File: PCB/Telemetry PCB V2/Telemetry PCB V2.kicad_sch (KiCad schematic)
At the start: 47 parts, among them IC1 E22-900M22S, J1 USB_C_Receptacle_USB2.0_16P, J2 DBG/PGRM Hdr., J3 DATA IN, J4 GPS, J5 Battery, SW1 SW_MEC_5E, SW2 SW_MEC_5E, U1 STM32F411CEUx, U2 MCP1700x-250xxTT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

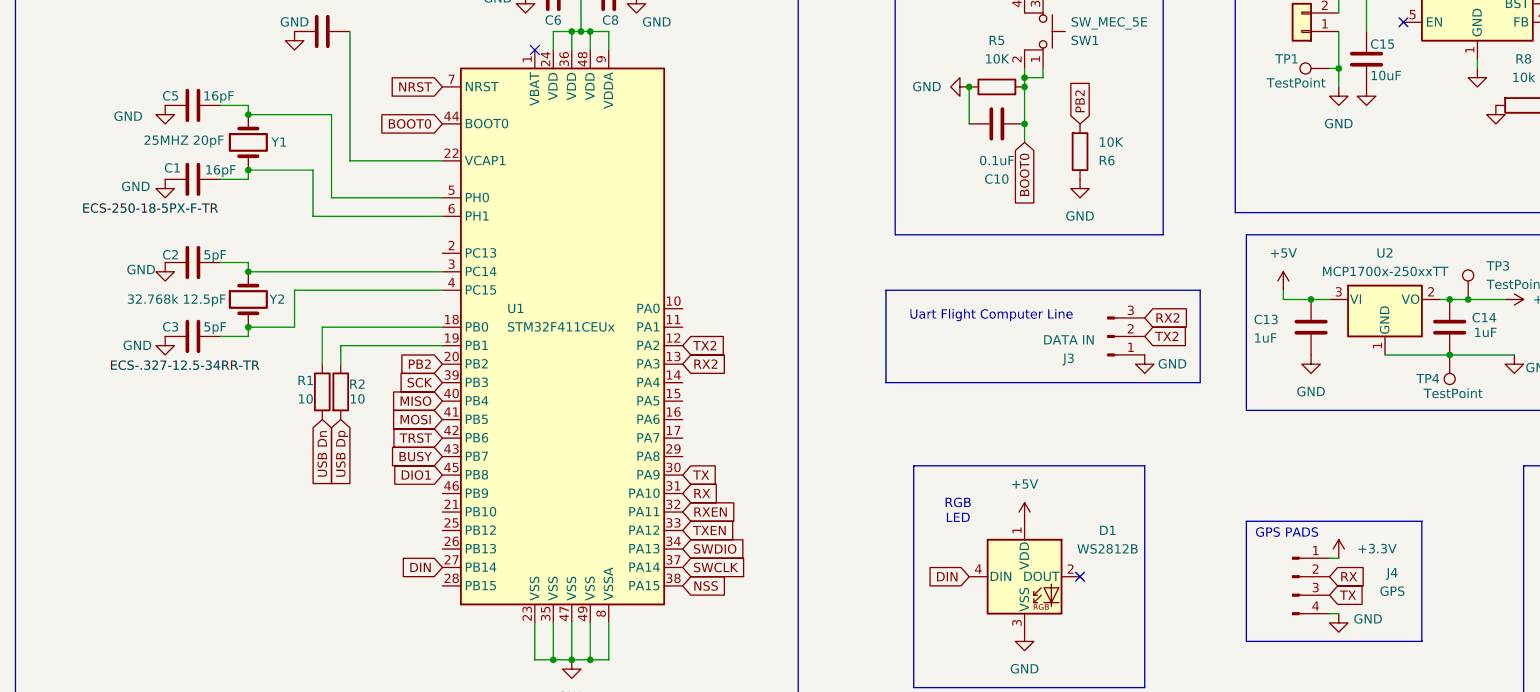
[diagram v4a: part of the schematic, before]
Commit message: Changed GPS power to 5V
Changed GPS power to 5V because I was not sure what it's current draw is and we don't have a ton of spare capacity on the 3.3V power regulator. Powering of of 5V is also likely more power efficient as it is not passing through a linear voltage regulator
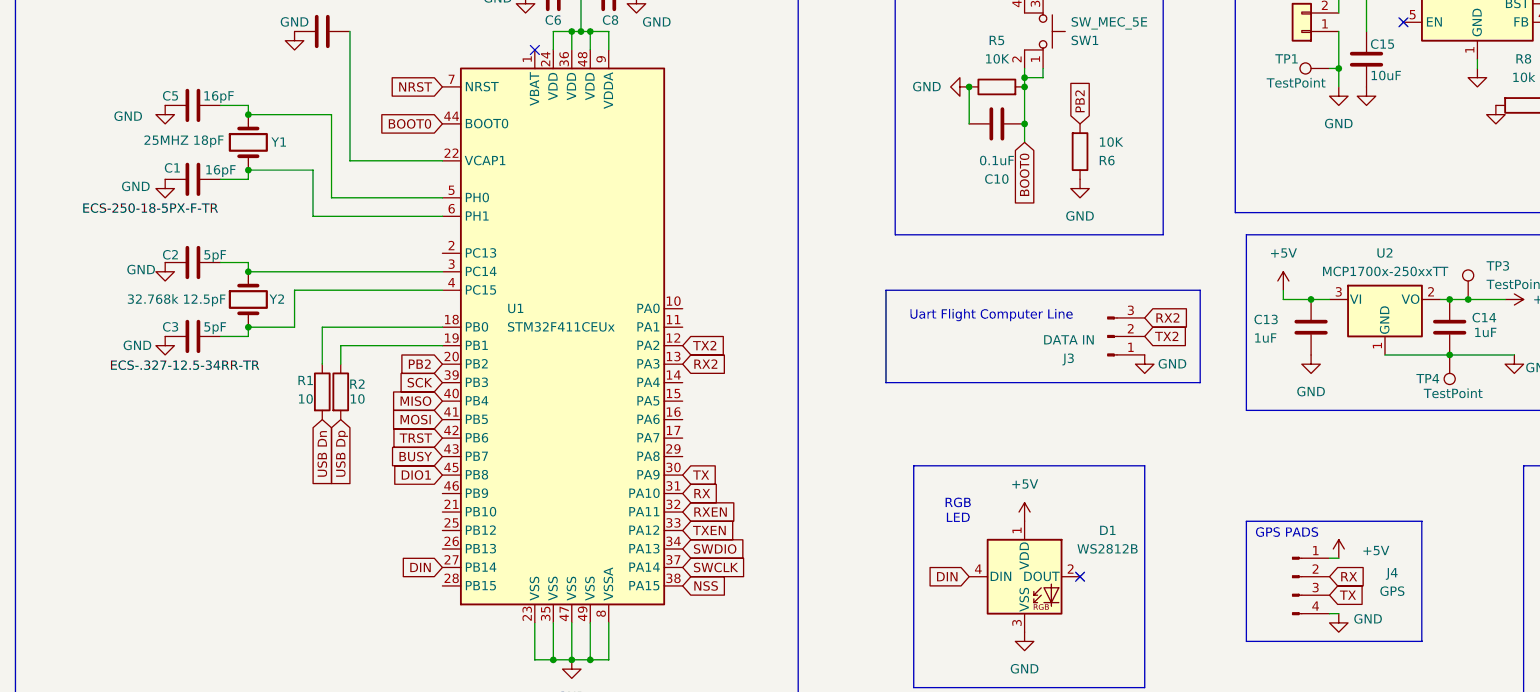
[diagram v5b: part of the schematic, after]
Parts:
- Y1: value 25MHZ 20pF -> 25MHZ 18pF
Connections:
- net +3.3V: no longer J4.1 (Pin_1)
- net +5V: now also J4.1 (Pin_1)
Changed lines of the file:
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@@
 			)
 		)
-		(property "Value" "25MHZ 20pF"
+		(property "Value" "25MHZ 18pF"
 			(at 53.848 48.006 90)
 			(effects
@@
 	)
 	(symbol
+		(lib_id "power:+5V")
+		(at 207.01 105.41 0)
+		(unit 1)
+		(exclude_from_sim no)
+		(in_bom yes)
+		(on_board yes)
+		(dnp no)
+		(property "Reference" "#PWR011"
+			(at 207.01 109.22 0)
+			(effects
+				(font
+					(size 1.27 1.27)
+				)
+				(hide yes)
+			)
+		)
+		(property "Value" "+5V"
+			(at 212.09 104.394 0)
+			(effects
+				(font
+					(size 1.27 1.27)
+				)
+			)
+		)
+		(property "Footprint" ""
+			(at 207.01 105.41 0)
+			(effects
+				(font
+					(size 1.27 1.27)
+				)
+				(hide yes)
+			)
+		)
+		(property "Datasheet" ""
+			(at 207.01 105.41 0)
+			(effects
+				(font
+					(size 1.27 1.27)
+				)
+				(hide yes)
+			)
+		)
+		(property "Description" "Power symbol creates a global label with name \"+5V\""
+			(at 207.01 105.41 0)
+			(effects
+				(font
+					(size 1.27 1.27)
+				)
+				(hide yes)
+			)
+		)
+		(pin "1"
+		)
+		(instances
+			(project ""
+				(path "/d3e58202-7594-4bd8-a3d4-cb0300333d9c"
+					(reference "#PWR011")
+					(unit 1)
+				)
+			)
+		)
+	)
+	(symbol
 		(lib_name "+3.3V_3")
 		(lib_id "power:+3.3V")
@@
 					(unit 1)
 				)
-			)
-		)
-	)
-	(symbol
-		(lib_name "+3.3V_6")
-		(lib_id "power:+3.3V")
-		(at 207.01 105.41 0)
-		(unit 1)
-		(exclude_from_sim no)
-		(in_bom yes)
-		(on_board yes)
-		(dnp no)
-		(fields_autoplaced yes)
-		(property "Reference" "#PWR034"
-			(at 207.01 109.22 0)
-			(effects
-				(font
-					(size 1.27 1.27)
-				)
-				(hide yes)
-			)
-		)
-		(property "Value" "+3.3V"
-			(at 209.55 104.1399 0)
-			(effects
-				(font
-					(size 1.27 1.27)
-				)
-				(justify left)
-			)
-		)
-		(property "Footprint" ""
-			(at 207.01 105.41 0)
-			(effects
-				(font
-					(size 1.27 1.27)
-				)
-				(hide yes)
-			)
-		)
-		(property "Datasheet" ""
-			(at 207.01 105.41 0)
-			(effects
-				(font
-					(size 1.27 1.27)
-				)
-				(hide yes)
-			)
-		)
-		(property "Description" "Power symbol creates a global label with name \"+3.3V\""
-			(at 207.01 105.41 0)
-			(effects
-				(font
-					(size 1.27 1.27)
-				)
-				(hide yes)
-			)
-		)
-		(pin "1"
-		)
-		(instances
-			(project ""
-				(path "/d3e58202-7594-4bd8-a3d4-cb0300333d9c"
-					(reference "#PWR034")
-					(unit 1)
-				)

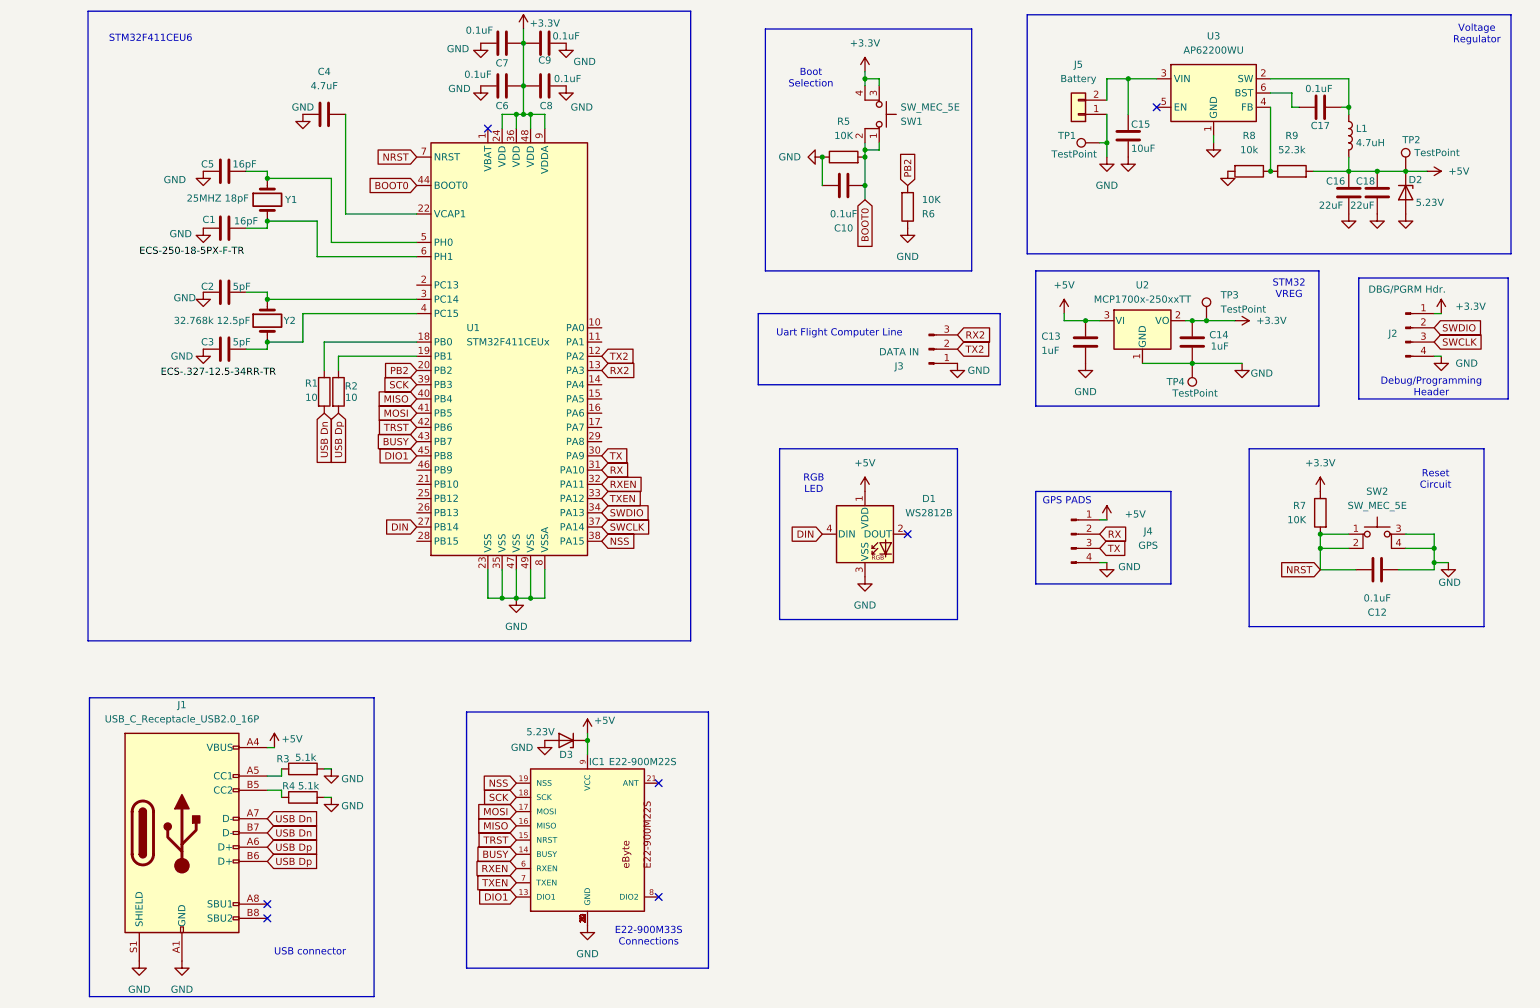
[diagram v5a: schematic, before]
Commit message: Changed schematic to reflect issues found, started to modify board layout.
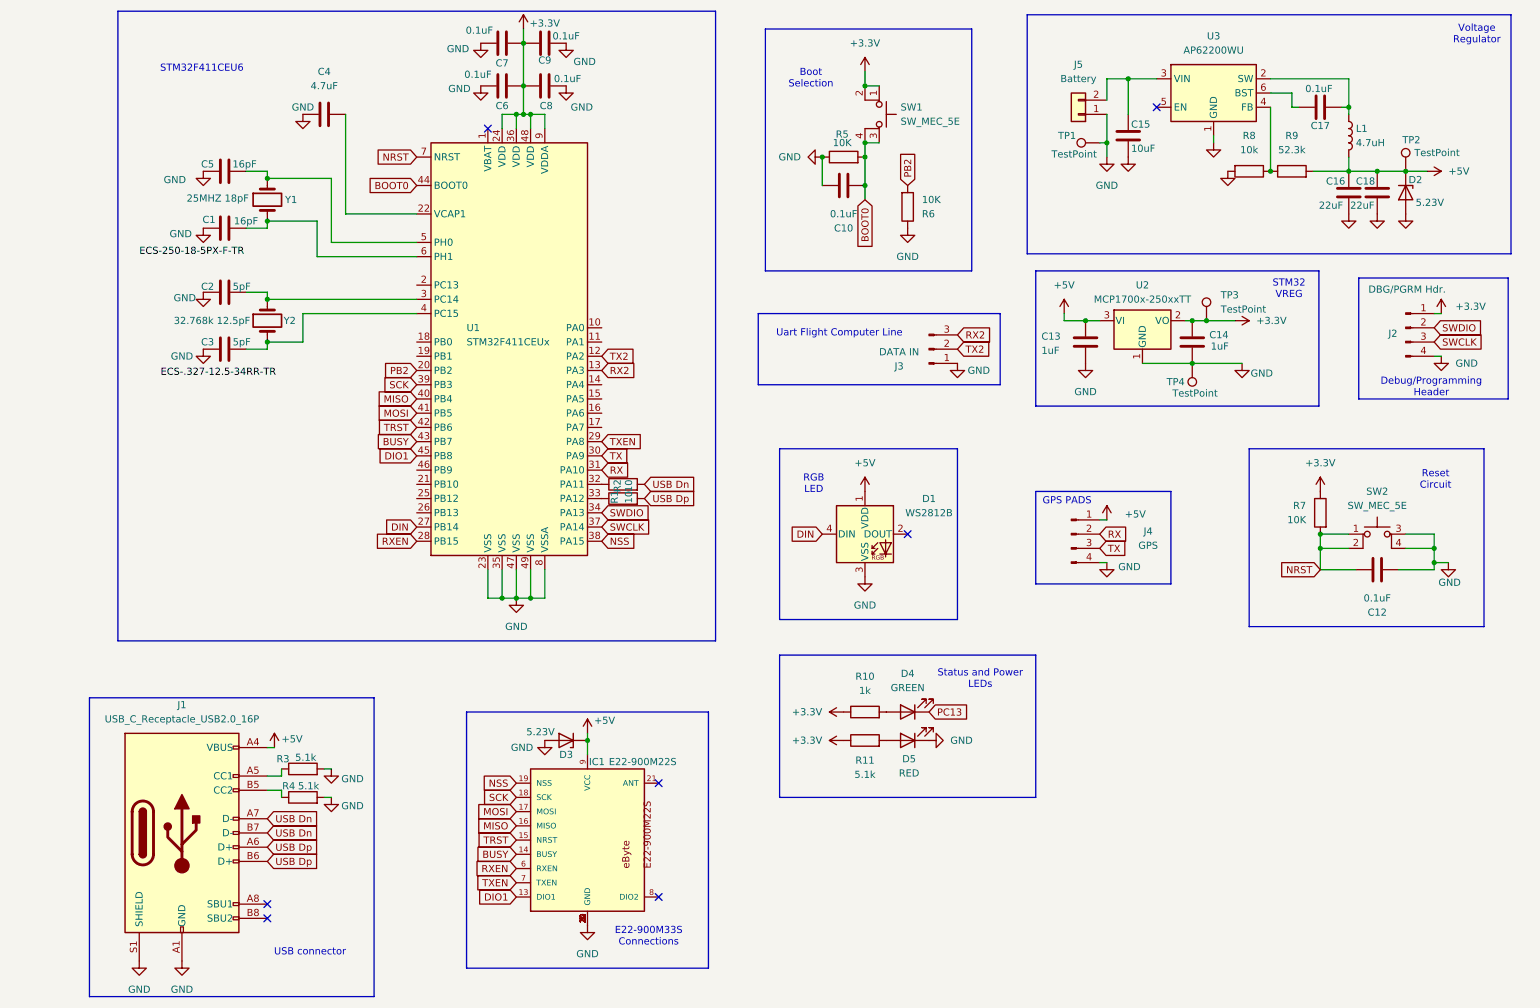
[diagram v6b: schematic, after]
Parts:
- added D4: GREEN, LED_SMD:LED_1206_3216Metric, symbol Device:LED
- added D5: RED, LED_SMD:LED_1206_3216Metric, symbol Device:LED
- added R10: 1k, Resistor_SMD:R_1206_3216Metric, symbol Device:R
- added R11: 5.1k, Resistor_SMD:R_1206_3216Metric, symbol Device:R
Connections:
- net +3.3V: now also SW1.1, SW1.2, R10.1, R11.1; no longer SW1.3 (A), SW1.4 (K)
- net BOOT0: now also SW1.3 (A), SW1.4 (K); no longer SW1.1, SW1.2
- net GND: now also D5.1 (K)
- net RXEN: now also U1.28 (PB15); no longer U1.32 (PA11)
- net TXEN: now also U1.29 (PA8); no longer U1.33 (PA12)
- net at U1.18 (PB0): no longer R1.1
- net at U1.19 (PB1): no longer R2.1
- new net: R1.1, U1.32 (PA11)
- new net: R2.1, U1.33 (PA12)
- new net: D5.2 (A), R11.2
- new net: D4.2 (A), R10.2
- new net PC13: D4.1 (K)
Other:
- note added: "Status and Power LEDs"
- moved on the sheet: R1, R2

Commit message: Finished updating board to reflect issues and new components
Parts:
- SW1: value SW_MEC_5E -> BOOT
- SW2: value SW_MEC_5E -> RESET
- TP1, TP4: value TestPoint -> GND
- TP2: value TestPoint -> +5v
- TP3: value TestPoint -> 3.3v
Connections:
- net PC13: now also U1.2 (PC13)
- net RX: now also U1.26 (PB13); no longer U1.31 (PA10)
- net TX: now also U1.25 (PB12); no longer U1.30 (PA9)
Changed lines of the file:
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@@
 	(global_label "RX"
 		(shape input)
-		(at 116.84 96.52 0)
+		(at 83.82 104.14 180)
 		(fields_autoplaced yes)
 		(effects
@@
 				(size 1.27 1.27)
 			)
-			(justify left)
+			(justify right)
 		)
 		(property "Intersheetrefs" "${INTERSHEET_REFS}"
-			(at 122.3047 96.52 0)
+			(at 78.3553 104.14 0)
 			(effects
 				(font
 					(size 1.27 1.27)
 				)
-				(justify left)
+				(justify right)
 				(hide yes)
 			)
@@
 	(global_label "TX"
 		(shape input)
-		(at 116.84 93.98 0)
+		(at 83.82 101.6 180)
 		(fields_autoplaced yes)
 		(effects
@@
 				(size 1.27 1.27)
 			)
-			(justify left)
+			(justify right)
 		)
 		(property "Intersheetrefs" "${INTERSHEET_REFS}"
-			(at 122.0023 93.98 0)
+			(at 78.6577 101.6 0)
 			(effects
 				(font
 					(size 1.27 1.27)
 				)
-				(justify left)
+				(justify right)
 				(hide yes)
 			)
@@
 		)
 	)
+	(global_label "PC13"
+		(shape input)
+		(at 83.82 63.5 180)
+		(fields_autoplaced yes)
+		(effects
+			(font
+				(size 1.27 1.27)
+			)
+			(justify right)
+		)
+		(property "Intersheetrefs" "${INTERSHEET_REFS}"
+			(at 75.8758 63.5 0)
+			(effects
+				(font
+					(size 1.27 1.27)
+				)
+				(justify right)
+				(hide yes)
+			)
+		)
+	)
 	(global_label "NRST"
 		(shape input)
@@
 			)
 		)
-		(property "Value" "TestPoint"
+		(property "Value" "GND"
 			(at 218.694 82.804 0)
 			(effects
@@
 			)
 		)
-		(property "Value" "TestPoint"
+		(property "Value" "GND"
 			(at 201.168 40.132 90)
 			(effects
@@
 			)
 		)
-		(property "Value" "SW_MEC_5E"
+		(property "Value" "BOOT"
 			(at 170.18 34.2899 90)
 			(effects
@@
 			)
 		)
-		(property "Value" "TestPoint"
+		(property "Value" "+5v"
 			(at 265.938 39.878 0)
 			(effects
@@
 			)
 		)
-		(property "Value" "SW_MEC_5E"
+		(property "Value" "RESET"
 			(at 255.27 102.87 0)
 			(effects
@@
 			)
 		)
-		(property "Value" "TestPoint"
+		(property "Value" "3.3v"
 			(at 227.33 67.8179 0)
 			(effects

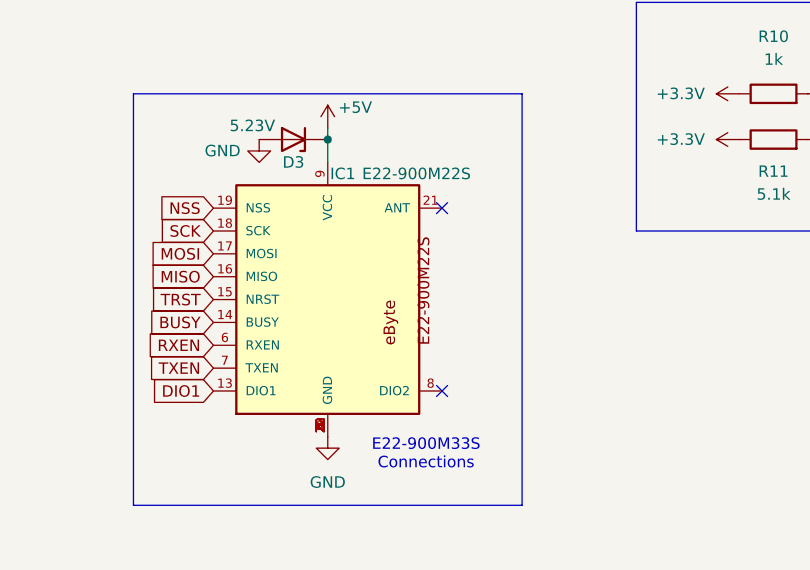
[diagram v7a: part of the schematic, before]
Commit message: V 2.2 Updated Incorrect Pinout
The Transmitter pinout has been corrected.
Disregard previous message this will be The flight revision of the board.
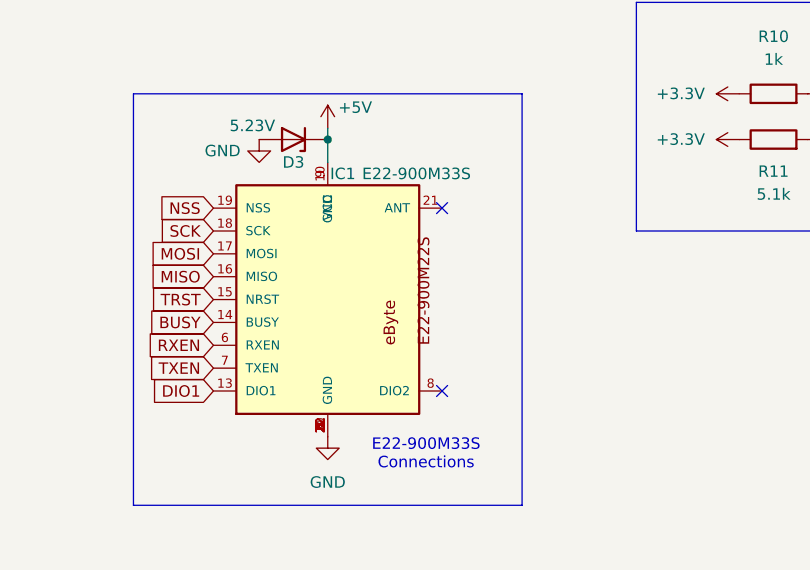
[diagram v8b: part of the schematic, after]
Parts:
- IC1: value E22-900M22S -> E22-900M33S; footprint E22-900M30S:XCVR_E22-900M30S -> E22-900M33S:XCVR_E22-900M33S
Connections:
- net +5V: now also IC1.10 (GND)
- net GND: no longer IC1.10 (GND)
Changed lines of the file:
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@@
 			)
 		)
-		(property "Value" "E22-900M22S"
+		(property "Value" "E22-900M33S"
 			(at 118.11 148.59 0)
 			(effects
@@
 			)
 		)
-		(property "Footprint" "E22-900M30S:XCVR_E22-900M30S"
+		(property "Footprint" "E22-900M33S:XCVR_E22-900M33S"
 			(at 114.3 162.56 0)
 			(effects
